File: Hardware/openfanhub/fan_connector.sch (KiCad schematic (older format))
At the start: 6 parts, among them M1 Fan_4pin, Q4 Q_PMOS_DGS

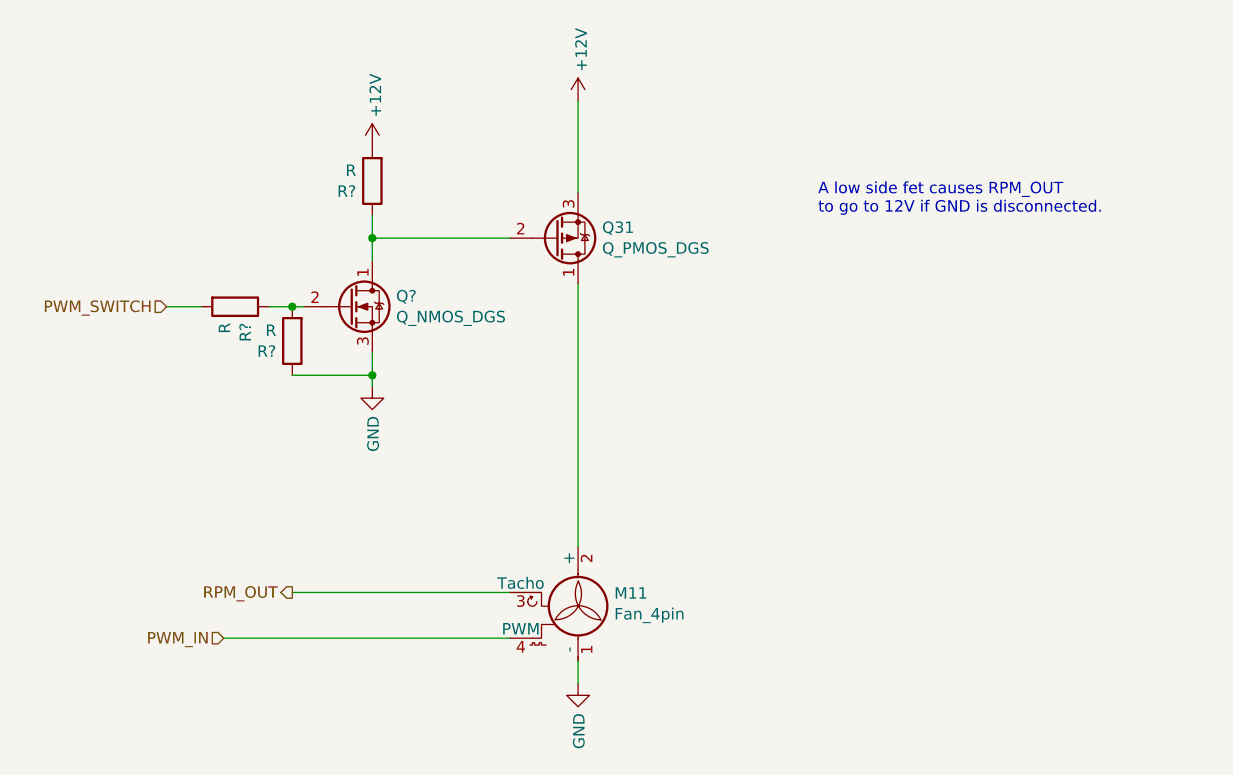
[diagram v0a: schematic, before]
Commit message: Enable fan by default (even if µC is offline)
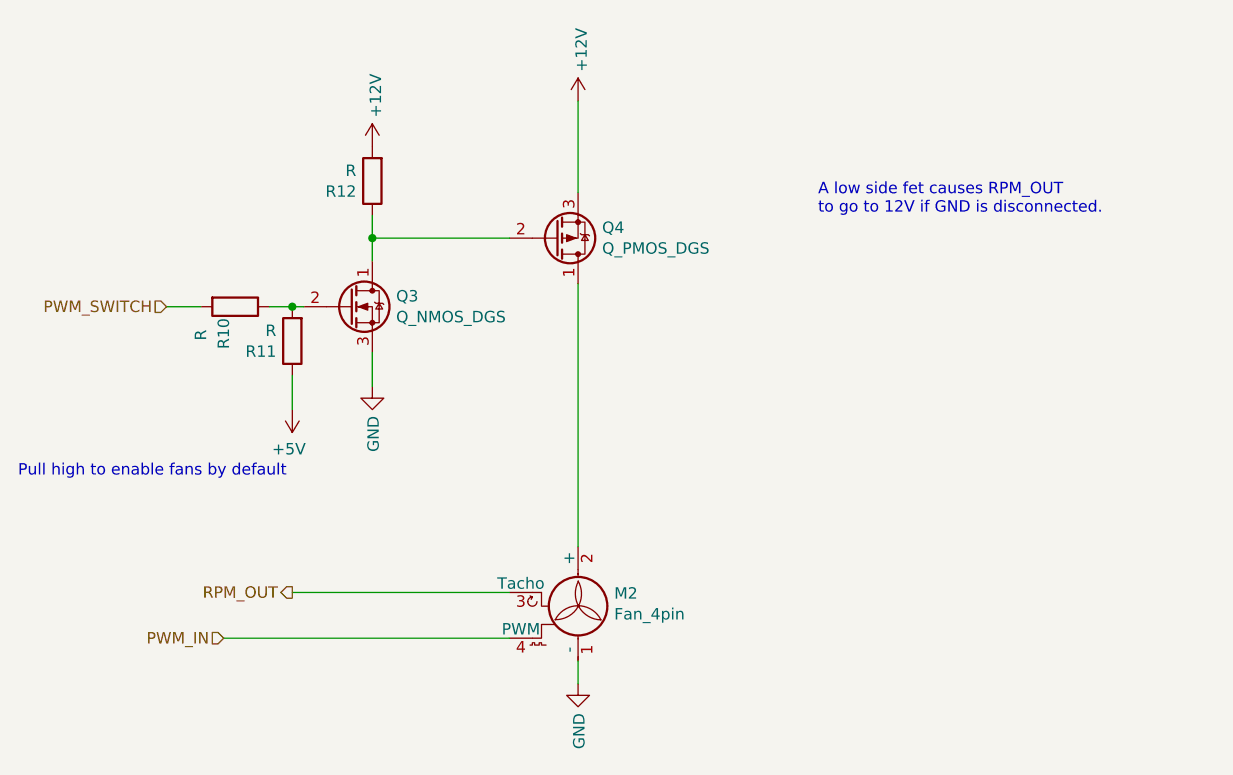
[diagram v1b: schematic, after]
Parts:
- gave numbers to parts that had none: 4
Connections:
- net GND: no longer R8.1
- new net +5V: R8.1
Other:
- note added: "Pull high to enable fans by default\n"

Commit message: Update files to kicad 6
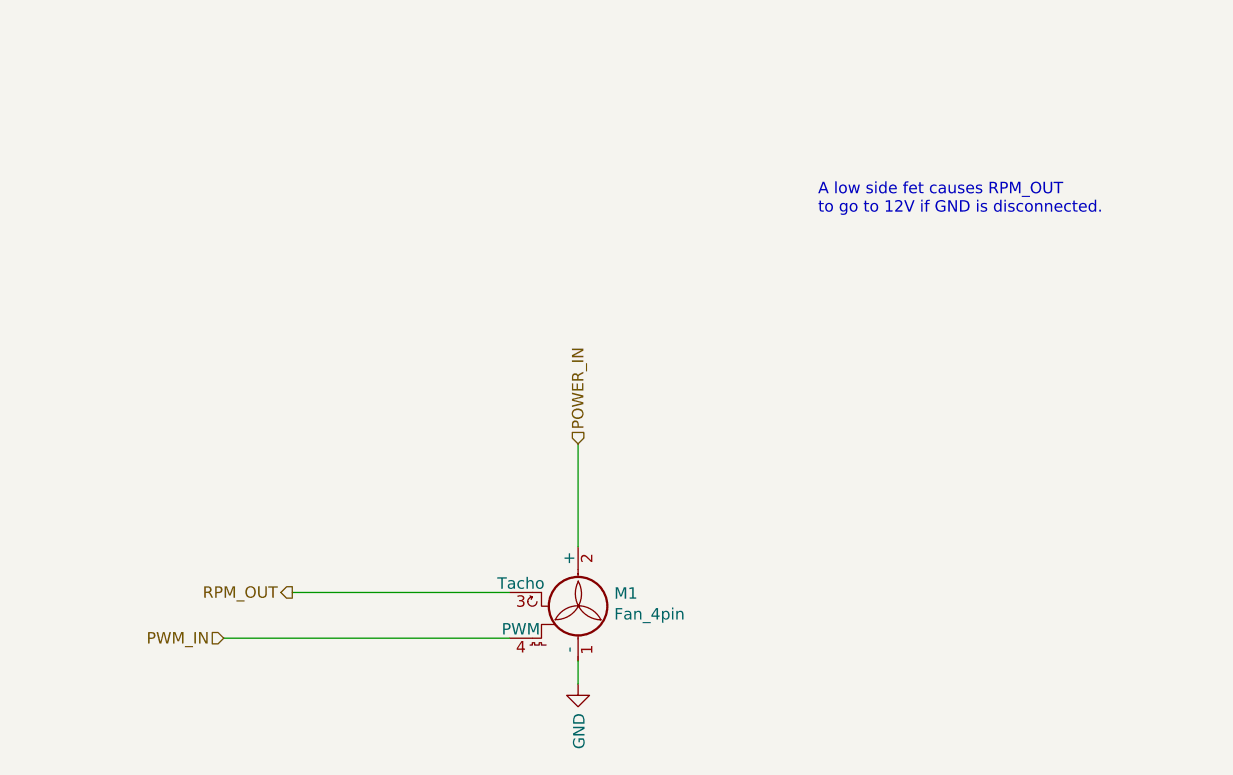
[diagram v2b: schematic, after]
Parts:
- removed Q17: Q_NMOS_DGS, symbol Device:Q_NMOS_DGS
- removed Q4: Q_PMOS_DGS, symbol Device:Q_PMOS_DGS
- removed R5, R8, R9: R, symbol Device:R
- M1: footprint (none) -> Connector_PinHeader_2.54mm:PinHeader_1x04_P2.54mm_Horizontal
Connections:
- net POWER_IN: now reaches M1.2 (+)
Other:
- note removed: "Pull high to enable fans by default\n"
